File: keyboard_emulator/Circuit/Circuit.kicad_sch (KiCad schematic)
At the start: 9 parts, among them J1 Screw_Terminal_01x02, J2 Screw_Terminal_01x02, J3 Screw_Terminal_01x02, J4 Screw_Terminal_01x02, SW1 SW_Push, SW2 SW_Push, SW3 SW_Push, SW4 SW_Push, U1 Sparkfun_Pro_Micro

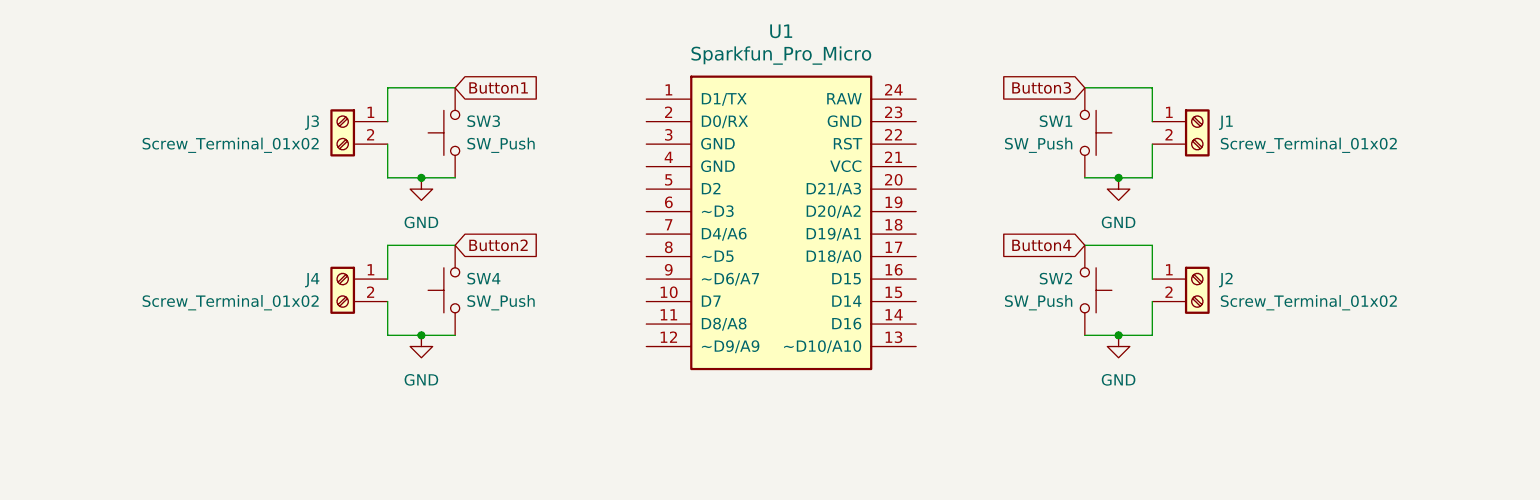
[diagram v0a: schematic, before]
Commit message: finished keyboard emulator circuit and some BOMs
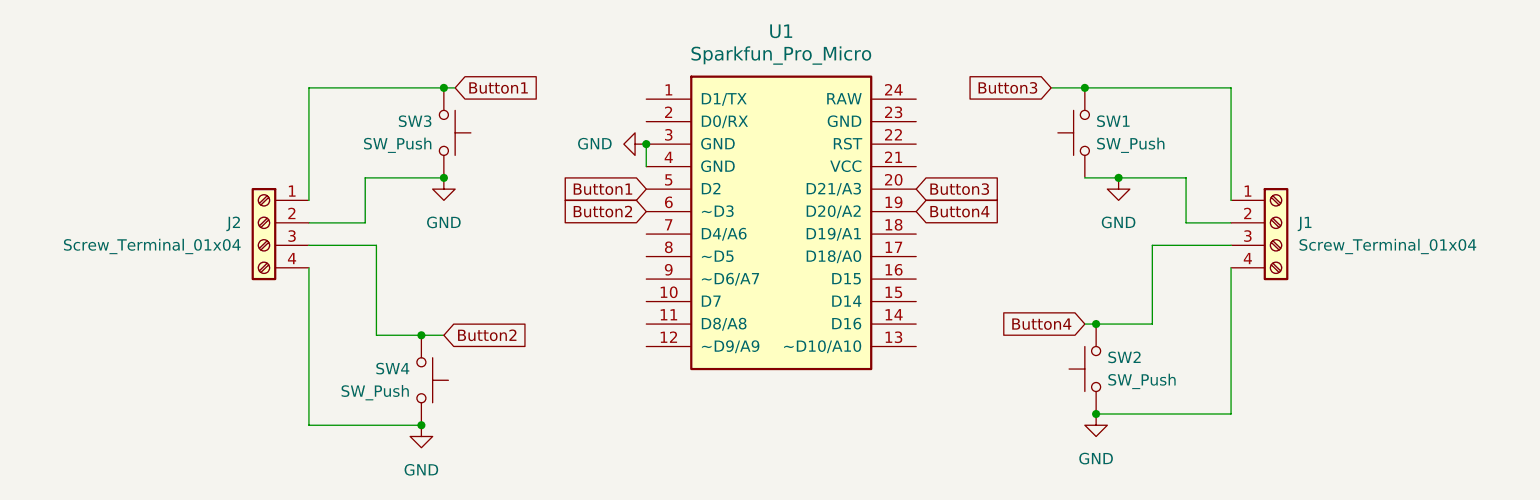
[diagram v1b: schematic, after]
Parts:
- removed J1, J2, J3, J4: Screw_Terminal_01x02, symbol Connector:Screw_Terminal_01x02
- added J1, J2: Screw_Terminal_01x04, speaker_terminal_spring:speaker_terminal_spring_4, symbol Connector:Screw_Terminal_01x04
- SW1, SW2, SW3, SW4: footprint (none) -> push_button_big_oval:push_button_oval
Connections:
- net Button1: now also U1.5 (D2), J2.1 (Pin_1)
- net Button2: now also U1.6 (~D3), J2.3 (Pin_3)
- net Button3: now also U1.20 (D21/A3), J1.1 (Pin_1)
- net Button4: now also U1.19 (D20/A2), J1.3 (Pin_3)
- net GND: now also U1.3 (GND), U1.4 (GND), J1.2 (Pin_2), J1.4 (Pin_4), J2.2 (Pin_2), J2.4 (Pin_4)

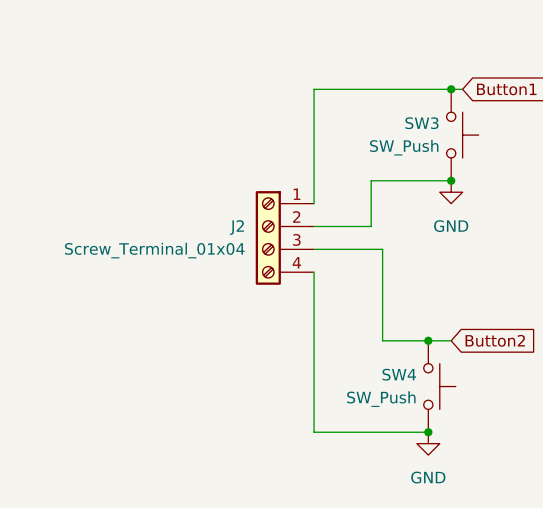
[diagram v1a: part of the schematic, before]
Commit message: added step files for keyboard emulator
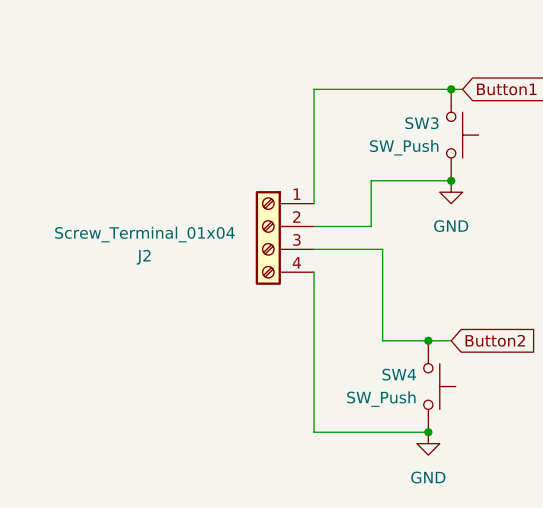
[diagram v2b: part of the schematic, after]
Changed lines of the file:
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@@
+	(wire
+		(pts
+			(xy 92.71 114.3) (xy 92.71 132.08)
+		)
+		(stroke
+			(width 0)
+			(type default)
+		)
+	)
 	(wire
 		(pts
@@
 		(pts
 			(xy 184.15 104.14) (xy 180.34 104.14)
-		)
-		(stroke
-			(width 0)
-			(type default)
-		)
-	)
-	(wire
-		(pts
-			(xy 92.71 114.3) (xy 92.71 132.08)
 		)
 		(stroke
@@
 		(dnp no)
 		(property "Reference" "J2"
-			(at 85.09 109.2199 0)
-			(effects
-				(font
-					(size 1.27 1.27)
-				)
-				(justify left)
+			(at 73.914 112.522 0)
+			(effects
+				(font
+					(size 1.27 1.27)
+				)
 			)
 		)
 		(property "Value" "Screw_Terminal_01x04"
-			(at 85.09 111.7599 0)
-			(effects
-				(font
-					(size 1.27 1.27)
-				)
-				(justify left)
-			)
-		)
+			(at 73.914 109.982 0)
+			(effects
+				(font
+					(size 1.27 1.27)
+				)
+			)
+		)
